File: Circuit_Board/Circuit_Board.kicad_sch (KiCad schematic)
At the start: 17 parts, among them J1 Conn_01x02, J2 Control stuff, J3 Power stuff, J4 Conn_02x06_Odd_Even, U1 Pico

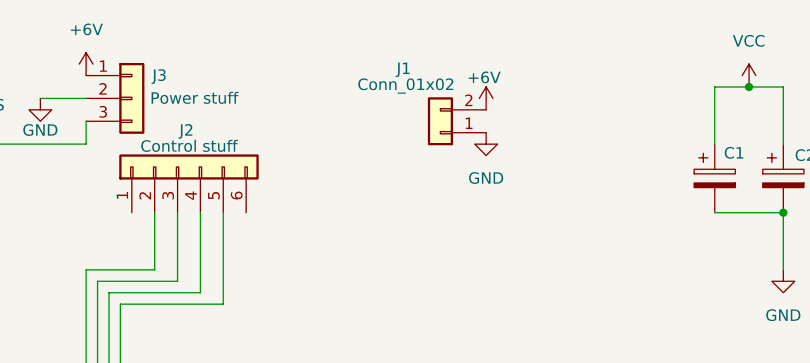
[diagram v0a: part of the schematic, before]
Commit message: Started work on pcb lay and add input pins vars to main
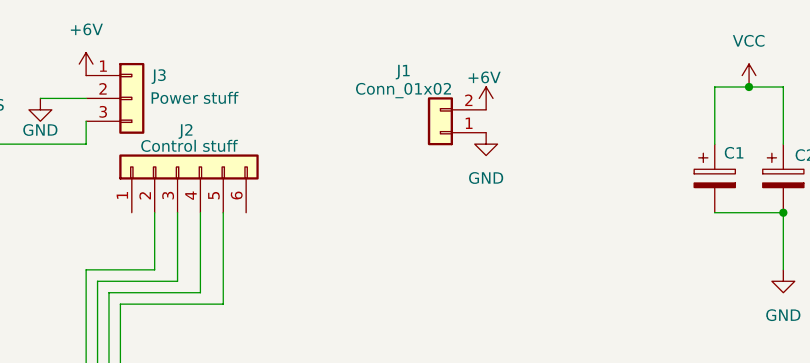
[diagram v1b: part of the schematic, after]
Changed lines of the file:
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@@
 		)
 		(instances
-			(project "Circuit Board"
+			(project "Circuit_Board"
 				(path "/4ae8f7b1-f10b-4627-ad62-bdeaaafef58f"
 					(reference "IR2")
@@
 		)
 		(instances
-			(project "Circuit Board"
+			(project "Circuit_Board"
 				(path "/4ae8f7b1-f10b-4627-ad62-bdeaaafef58f"
 					(reference "#PWR09")
@@
 		)
 		(instances
-			(project "Circuit Board"
+			(project "Circuit_Board"
 				(path "/4ae8f7b1-f10b-4627-ad62-bdeaaafef58f"
 					(reference "#PWR014")
@@
 		)
 		(instances
-			(project "Circuit Board"
+			(project "Circuit_Board"
 				(path "/4ae8f7b1-f10b-4627-ad62-bdeaaafef58f"
 					(reference "#PWR01")
@@
 		)
 		(instances
-			(project "Circuit Board"
+			(project "Circuit_Board"
 				(path "/4ae8f7b1-f10b-4627-ad62-bdeaaafef58f"
 					(reference "#PWR05")
@@
 		)
 		(instances
-			(project "Circuit Board"
+			(project "Circuit_Board"
 				(path "/4ae8f7b1-f10b-4627-ad62-bdeaaafef58f"
 					(reference "#PWR08")
@@
 		)
 		(instances
-			(project "Circuit Board"
+			(project "Circuit_Board"
 				(path "/4ae8f7b1-f10b-4627-ad62-bdeaaafef58f"
 					(reference "R3")
@@
 		)
 		(instances
-			(project "Circuit Board"
+			(project "Circuit_Board"
 				(path "/4ae8f7b1-f10b-4627-ad62-bdeaaafef58f"
 					(reference "#PWR010")
@@
 		)
 		(instances
-			(project "Circuit Board"
+			(project "Circuit_Board"
 				(path "/4ae8f7b1-f10b-4627-ad62-bdeaaafef58f"
 					(reference "R2")
@@
 		)
 		(instances
-			(project "Circuit Board"
+			(project "Circuit_Board"
 				(path "/4ae8f7b1-f10b-4627-ad62-bdeaaafef58f"
 					(reference "#PWR017")
@@
 		)
 		(instances
-			(project "Circuit Board"
+			(project "Circuit_Board"
 				(path "/4ae8f7b1-f10b-4627-ad62-bdeaaafef58f"
 					(reference "C2")
@@
 		)
 		(instances
-			(project "Circuit Board"
+			(project "Circuit_Board"
 				(path "/4ae8f7b1-f10b-4627-ad62-bdeaaafef58f"
 					(reference "#PWR015")
@@
 		)
 		(instances
-			(project "Circuit Board"
+			(project "Circuit_Board"
 				(path "/4ae8f7b1-f10b-4627-ad62-bdeaaafef58f"
 					(reference "J2")
@@
 		)
 		(instances
-			(project "Circuit Board"
+			(project "Circuit_Board"
 				(path "/4ae8f7b1-f10b-4627-ad62-bdeaaafef58f"
 					(reference "#PWR03")
@@
 		)
 		(instances
-			(project "Circuit Board"
+			(project "Circuit_Board"
 				(path "/4ae8f7b1-f10b-4627-ad62-bdeaaafef58f"
 					(reference "#PWR011")
@@
 		)
 		(instances
-			(project "Circuit Board"
+			(project "Circuit_Board"
 				(path "/4ae8f7b1-f10b-4627-ad62-bdeaaafef58f"
 					(reference "#PWR012")
@@
 		)
 		(instances
-			(project "Circuit Board"
+			(project "Circuit_Board"
 				(path "/4ae8f7b1-f10b-4627-ad62-bdeaaafef58f"
 					(reference "C1")
@@
 		)
 		(instances
-			(project "Circuit Board"
+			(project "Circuit_Board"
 				(path "/4ae8f7b1-f10b-4627-ad62-bdeaaafef58f"
 					(reference "D1")
@@
 		)
 		(instances
-			(project "Circuit Board"
+			(project "Circuit_Board"
 				(path "/4ae8f7b1-f10b-4627-ad62-bdeaaafef58f"
 					(reference "#PWR016")
@@
 		)
 		(instances
-			(project "Circuit Board"
+			(project "Circuit_Board"
 				(path "/4ae8f7b1-f10b-4627-ad62-bdeaaafef58f"
 					(reference "U1")
@@
 		)
 		(instances
-			(project "Circuit Board"
+			(project "Circuit_Board"
 				(path "/4ae8f7b1-f10b-4627-ad62-bdeaaafef58f"
 					(reference "#PWR04")
@@
 		)
 		(instances
-			(project "Circuit Board"
+			(project "Circuit_Board"
 				(path "/4ae8f7b1-f10b-4627-ad62-bdeaaafef58f"
 					(reference "#PWR06")
@@
 		)
 		(instances
-			(project "Circuit Board"
+			(project "Circuit_Board"
 				(path "/4ae8f7b1-f10b-4627-ad62-bdeaaafef58f"
 					(reference "R1")
@@
 		)
 		(instances
-			(project "Circuit Board"
+			(project "Circuit_Board"
 				(path "/4ae8f7b1-f10b-4627-ad62-bdeaaafef58f"
 					(reference "#PWR013")
@@
 		)
 		(instances
-			(project "Circuit Board"
+			(project "Circuit_Board"
 				(path "/4ae8f7b1-f10b-4627-ad62-bdeaaafef58f"
 					(reference "#PWR07")
@@
 		)
 		(instances
-			(project "Circuit Board"
+			(project "Circuit_Board"
 				(path "/4ae8f7b1-f10b-4627-ad62-bdeaaafef58f"
 					(reference "J4")
@@
 		)
 		(instances
-			(project "Circuit Board"
+			(project "Circuit_Board"
 				(path "/4ae8f7b1-f10b-4627-ad62-bdeaaafef58f"
 					(reference "IR1")
@@
 		(dnp no)
 		(property "Reference" "J1"
-			(at 153.416 38.608 0)
+			(at 153.416 38.862 0)
 			(show_name no)
 			(do_not_autoplace no)
@@
 		)
 		(property "Value" "Conn_01x02"
-			(at 153.67 40.386 0)
+			(at 153.416 40.894 0)
 			(show_name no)
 			(do_not_autoplace no)
@@
 		)
 		(instances
-			(project "Circuit Board"
+			(project "Circuit_Board"
 				(path "/4ae8f7b1-f10b-4627-ad62-bdeaaafef58f"
 					(reference "J1")
@@
 		)
 		(instances
-			(project "Circuit Board"
+			(project "Circuit_Board"
 				(path "/4ae8f7b1-f10b-4627-ad62-bdeaaafef58f"
 					(reference "R4")
@@
 		)
 		(instances
-			(project "Circuit Board"
+			(project "Circuit_Board"
 				(path "/4ae8f7b1-f10b-4627-ad62-bdeaaafef58f"
 					(reference "C3")
@@
 		)
 		(instances
-			(project "Circuit Board"
+			(project "Circuit_Board"
 				(path "/4ae8f7b1-f10b-4627-ad62-bdeaaafef58f"
 					(reference "#PWR02")
@@
 		)
 		(instances
-			(project "Circuit Board"
+			(project "Circuit_Board"
 				(path "/4ae8f7b1-f10b-4627-ad62-bdeaaafef58f"
 					(reference "IR3")
@@
 		)
 		(instances
-			(project "Circuit Board"
+			(project "Circuit_Board"
 				(path "/4ae8f7b1-f10b-4627-ad62-bdeaaafef58f"
 					(reference "#PWR018")
@@
 		)
 		(instances
-			(project "Circuit Board"
+			(project "Circuit_Board"
 				(path "/4ae8f7b1-f10b-4627-ad62-bdeaaafef58f"
 					(reference "C4")
@@
 		)
 		(instances
-			(project "Circuit Board"
+			(project "Circuit_Board"
 				(path "/4ae8f7b1-f10b-4627-ad62-bdeaaafef58f"
 					(reference "J3")

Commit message: Changed board design
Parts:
- added D2, D3, D4: LED, LED_SMD:LED_0603_1608Metric_Pad1.05x0.95mm_HandSolder, symbol Device:LED
- added J5, J6: Conn_01x20_Socket, Connector_PinSocket_2.54mm:PinSocket_1x20_P2.54mm_Vertical, symbol Connector:Conn_01x20_Socket
- added J7, J8: Conn_01x04_Socket, Connector_JST:JST_XH_B4B-XH-A_1x04_P2.50mm_Vertical, symbol Connector:Conn_01x04_Socket
- added R5, R6, R7: R, Resistor_SMD:R_0603_1608Metric_Pad0.98x0.95mm_HandSolder, symbol Device:R
- added SW1, SW2: SW_Push, Button_Switch_SMD:SW_Push_1P1T_NO_Vertical_Wuerth_434133025816, symbol Switch:SW_Push
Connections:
- net GND: now also D2.1 (K), D3.1 (K), D4.1 (K), J6.3 (Pin_3), J7.4 (Pin_4), J8.4 (Pin_4)
- net VBUS: now also J6.1 (Pin_1)
- net VCC: now also J6.5 (Pin_5), J7.1 (Pin_1), J8.1 (Pin_1)
- net at IR2.2, R2.2, U1.32 (GPIO27_ADC1): now also J6.9 (Pin_9)
- net at IR1.2, R3.2, U1.31 (GPIO26_ADC0): now also J6.10 (Pin_10)
- net at J2.2 (Pin_2), U1.7 (GPIO5): now also J5.7 (Pin_7)
- net at J2.3 (Pin_3), U1.6 (GPIO4): now also J5.6 (Pin_6)
- net at J2.4 (Pin_4), U1.5 (GPIO3): now also J5.5 (Pin_5)
- net at J2.5 (Pin_5), U1.4 (GPIO2): now also J5.4 (Pin_4)
- net at D1.2 (A): now also U1.27 (GPIO21), J6.14 (Pin_14); no longer U1.21 (GPIO16)
- net at U1.1 (GPIO0): now also J5.1 (Pin_1)
- net at U1.10 (GPIO7): now also J5.10 (Pin_10)
- net at U1.11 (GPIO8): now also J5.11 (Pin_11)
- net at U1.12 (GPIO9): now also J5.12 (Pin_12)
- net at U1.13 (GND): now also J5.13 (Pin_13)
- net at U1.14 (GPIO10): now also J5.14 (Pin_14)
- net at U1.15 (GPIO11): now also J5.15 (Pin_15), SW1.2
- net at U1.16 (GPIO12): now also J5.16 (Pin_16), SW2.2
- net at U1.17 (GPIO13): now also J5.17 (Pin_17), R5.2
- net at U1.18 (GND): now also J5.18 (Pin_18)
- net at U1.19 (GPIO14): now also J5.19 (Pin_19), R6.2
- net at U1.2 (GPIO1): now also J5.2 (Pin_2)
- net at U1.20 (GPIO15): now also J5.20 (Pin_20), R7.2
- net at U1.22 (GPIO17): now also J6.19 (Pin_19), J7.2 (Pin_2)
- net at U1.23 (GND): now also J6.18 (Pin_18)
- net at U1.24 (GPIO18): now also J6.17 (Pin_17), J8.3 (Pin_3)
- net at U1.25 (GPIO19): now also J6.16 (Pin_16), J8.2 (Pin_2)
- net at U1.26 (GPIO20): now also J6.15 (Pin_15)
- net at U1.28 (GND): now also J6.13 (Pin_13)
- net at U1.29 (GPIO22): now also J6.12 (Pin_12)
- net at U1.3 (GND): now also J5.3 (Pin_3)
- net at U1.30 (RUN): now also J6.11 (Pin_11)
- net at U1.33 (AGND): now also J6.8 (Pin_8)
- net at IR3.2, R1.2, U1.34 (GPIO28_ADC2): now also J6.7 (Pin_7)
- net at U1.35 (ADC_VREF): now also J6.6 (Pin_6)
- net at U1.37 (3V3_EN): now also J6.4 (Pin_4)
- net at U1.39 (VSYS): now also J6.2 (Pin_2)
- net at U1.8 (GND): now also J5.8 (Pin_8)
- net at U1.9 (GPIO6): now also J5.9 (Pin_9)
- new net: SW1.1, SW2.1
- new net: J6.20 (Pin_20), J7.3 (Pin_3), U1.21 (GPIO16)
- new net: D2.2 (A), R7.1
- new net: D3.2 (A), R6.1
- new net: D4.2 (A), R5.1
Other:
- note removed: "To-Do: ampilife multible ir leds"
- moved on the sheet: D1, IR1, IR2, IR3, J4, R1, R2, R3, R4

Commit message: v1.0 of board excluding the mounting holes
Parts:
- added C5, C6, C7, C8: C_Polarized, Capacitor_SMD:C_0805_2012Metric_Pad1.18x1.45mm_HandSolder, symbol Device:C_Polarized
- added H1, H2, H3, H4: MountingHole, MountingHole:MountingHole_3.2mm_M3, symbol Mechanical:MountingHole
- added J9: LED_AMP, Connector_JST:JST_XH_B4B-XH-A_1x04_P2.50mm_Vertical, symbol Connector:Conn_01x04_Socket
- added Q2: IRF540N, Package_TO_SOT_THT:TO-220-3_Vertical, symbol Transistor_FET:IRF540N
- added R8: R, Resistor_SMD:R_0603_1608Metric_Pad0.98x0.95mm_HandSolder, symbol Device:R
- added SW3: SW_Push, Button_Switch_SMD:SW_Push_1P1T_NO_E-Switch_TL3301NxxxxxG, symbol Switch:SW_Push
- J2: footprint Connector_JST:JST_XH_B6B-XH-AM_1x06_P2.50mm_Vertical -> Connector_JST:JST_XH_B6B-XH-A_1x06_P2.50mm_Vertical
- J7: value Conn_01x04_Socket -> GPIO_1
- J8: value Conn_01x04_Socket -> GPIO_2
- SW1, SW2: footprint Button_Switch_SMD:SW_Push_1P1T_NO_Vertical_Wuerth_434133025816 -> Button_Switch_SMD:SW_Push_1P1T_NO_E-Switch_TL3301NxxxxxG
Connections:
- net +6V: now also C8.1, J9.1 (Pin_1)
- net GND: now also SW1.1, SW2.1, C5.2, C6.2, C7.2, C8.2, Q2.3 (S), R8.1, SW3.1
- net VBUS: now also C6.1, C7.1, J9.2 (Pin_2)
- net VCC: now also C5.1, J9.3 (Pin_3)
- net at J5.15 (Pin_15), U1.15 (GPIO11): now also SW2.2; no longer SW1.2
- net FET_GATE: now reaches J6.15 (Pin_15), U1.26 (GPIO20)
- net FET_GATE: now also Q2.1 (G), R8.2
- net at J5.10 (Pin_10), U1.10 (GPIO7): now also J2.1 (Pin_1)
- net at J5.14 (Pin_14), U1.14 (GPIO10): now also SW1.2
- net at J5.16 (Pin_16), U1.16 (GPIO12): now also SW3.2; no longer SW2.2
- net at J5.4 (Pin_4), U1.4 (GPIO2): now also J2.6 (Pin_6); no longer J2.5 (Pin_5)
- net at J5.5 (Pin_5), U1.5 (GPIO3): now also J2.5 (Pin_5); no longer J2.4 (Pin_4)
- net at J5.6 (Pin_6), U1.6 (GPIO4): now also J2.4 (Pin_4); no longer J2.3 (Pin_3)
- net at J5.7 (Pin_7), U1.7 (GPIO5): now also J2.3 (Pin_3); no longer J2.2 (Pin_2)
- net at J5.9 (Pin_9), U1.9 (GPIO6): now also J2.2 (Pin_2)
- new net: J9.4 (Pin_4), Q2.2 (D)
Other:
- moved on the sheet: C1, C2, C3, C4, J7, J8, SW1, SW2

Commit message: finalized pcb layout
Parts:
- R4: value 100R -> 100k
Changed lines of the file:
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@@
 			)
 		)
-		(property "Value" "100R"
+		(property "Value" "100k"
 			(at 190.246 114.808 90)
 			(show_name no)

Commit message: Made final changes to schmatic and PCB
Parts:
- C7: value C_Polarized -> 0.1uF
- C8: value C_Polarized -> 0.33uF
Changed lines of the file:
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@@
 			)
 		)
-		(property "Value" "C_Polarized"
-			(at 261.62 42.2909 0)
-			(hide yes)
+		(property "Value" "0.33uF"
+			(at 262.382 39.37 0)
 			(show_name no)
 			(do_not_autoplace no)
@@
 			)
 		)
-		(property "Value" "C_Polarized"
-			(at 190.5 42.2909 0)
-			(hide yes)
+		(property "Value" "0.1uF"
+			(at 178.816 39.878 0)
 			(show_name no)
 			(do_not_autoplace no)

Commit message: PCB Rev 1.1: Resistor value and silkscreen corrections
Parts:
- R4: value 100k -> 100R
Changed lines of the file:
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@@
 			)
 		)
-		(property "Value" "100k"
+		(property "Value" "100R"
 			(at 190.246 114.808 90)
 			(show_name no)
